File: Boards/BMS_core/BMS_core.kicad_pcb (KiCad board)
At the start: 2 copper layers, 73.7 x 61 mm, 67 parts, among them IC1 ATMEGA16M1, J1 CONN_02X03, J2 B5B-PH-K-S, J3 NanoFit_2, J4 MicroFit_RA_V_2, J5 MM_F_VT_14, K1 G5Q-1A4-DC5-5V, Q1 SSM3K333R, T1 T_LAN_7490100111A, U1 MCP2561-E_SN, U101 TPS561201, U2 SN74LVC1G17, U3 LTC6820HMS, U4 MCP6001, U5 MCP6001, Y1 Crystal_SMD

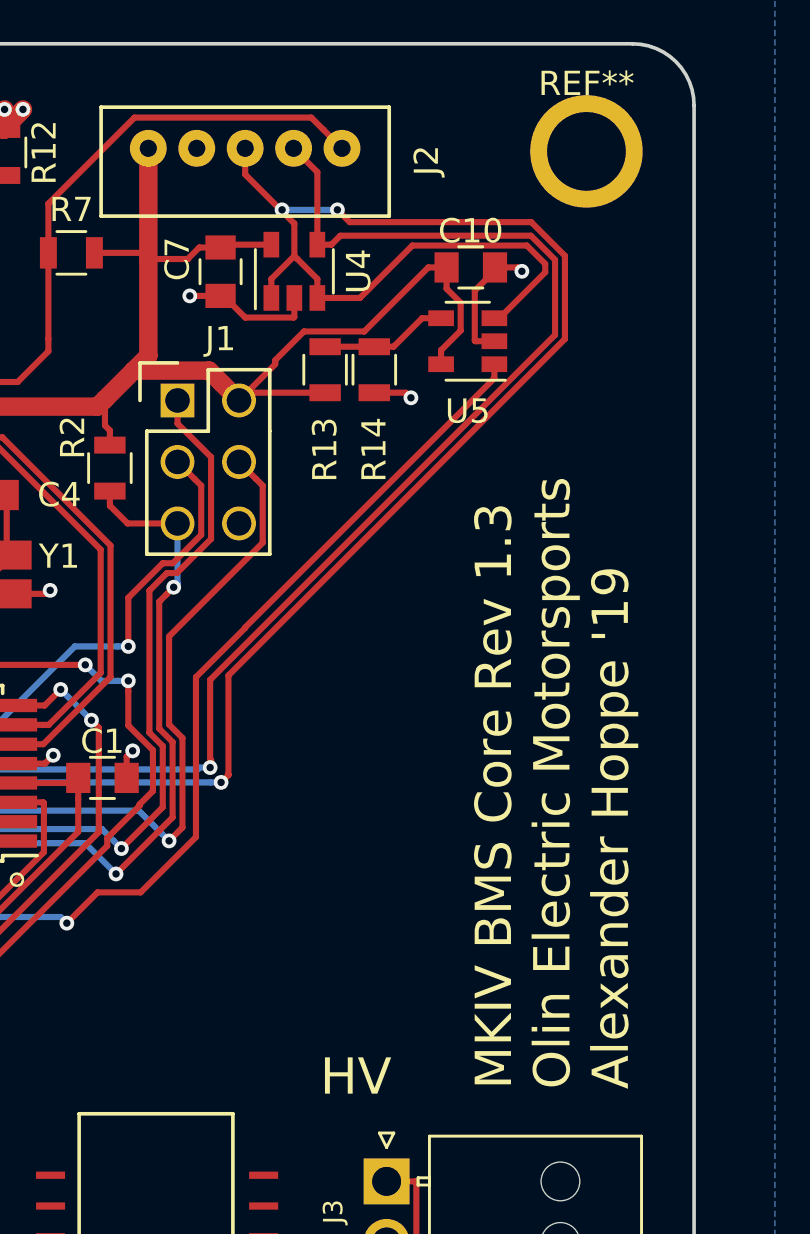
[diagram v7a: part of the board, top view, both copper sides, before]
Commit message: finished layout with new trigger
added components and ran clean DRC
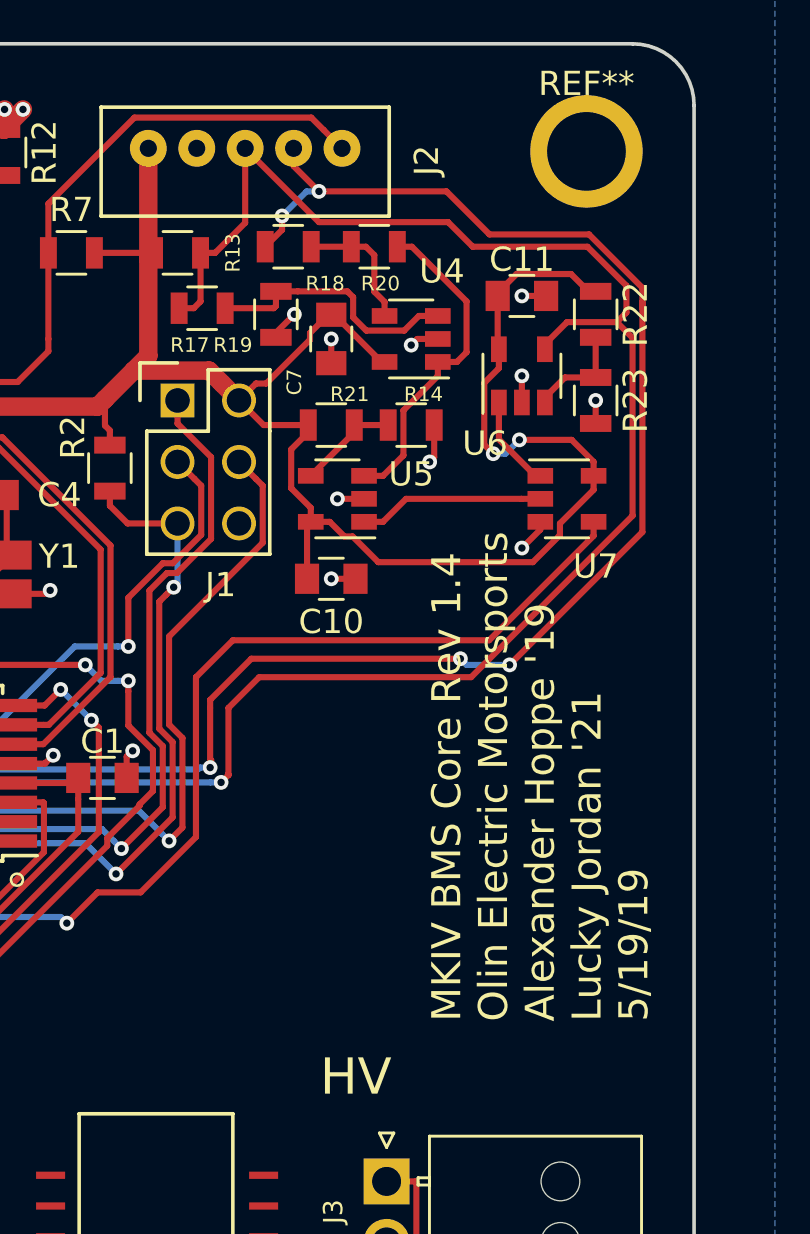
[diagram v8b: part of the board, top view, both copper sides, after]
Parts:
- added C11: C_0.1uF, footprints:C_0805_OEM, F.Cu at (109.7, 58.7)
- added R17: R_10K, footprints:R_0805_OEM, F.Cu at (96.5, 59.2)
- added R18: R_10K, footprints:R_0805_OEM, F.Cu at (100.1, 56.6)
- added R19: R_10K, footprints:R_0805_OEM, F.Cu at (99.6, 59.4)
- added R20: R_10K, footprints:R_0805_OEM, F.Cu at (103.6, 56.6)
- added R21: R_17.8K, footprints:R_0805_OEM, F.Cu at (101.9, 64.0)
- added R22: R_10K, footprints:R_0805_OEM, F.Cu at (112.8, 59.4)
- added R23: R_1K, footprints:R_0805_OEM, F.Cu at (112.8, 63.0)
- added U6: MCP6001, footprints:SOT-23-5_OEM, F.Cu at (109.7, 62.0)
- added U7: SN74LVC1G32, footprints:SOT-23-5_OEM, F.Cu at (111.6, 67.1)
- R13: value R_17.4K_0.1 -> R_10K
- moved C10 14.1 mm to (101.9, 70.4)
- moved U5 8.45 mm to (102.1, 67.1)
- moved R13 7.78 mm to (95.5, 56.9), turned to 180 degrees
- moved U4 5.58 mm to (105.2, 60.5), turned to 180 degrees
- moved C7 5.35 mm to (101.9, 60.5)
- moved R14 2.75 mm to (105.2, 64.0), turned to 0 degrees
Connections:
- R13 pad 1: VCC -> /VOUT
- R13 pad 2: Net-(R13-Pad2) -> VCC
- R14 pad 1: Net-(R13-Pad2) -> Net-(R14-Pad1)
- U4 pad 1: /VOUT -> Net-(R20-Pad2)
- U4 pad 3: /VOUT -> Net-(R17-Pad2)
- U4 pad 4: /VREF -> Net-(R18-Pad2)
- U5 pad 1: /BSPD_CURRENT -> Net-(U5-Pad1)
- U5 pad 3: /VOUT -> Net-(R20-Pad2)
- U5 pad 4: Net-(R13-Pad2) -> Net-(R14-Pad1)
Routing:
- net VCC: track 214.3 -> 240.5 mm, vias 5 -> 7
- net Net-(R20-Pad2): track 0.00 -> 13.7 mm
- net /VREF: track 59.5 -> 72.7 mm, vias 2 -> 6
- net Net-(R17-Pad2): track 0.00 -> 10.8 mm
- net Net-(U5-Pad1): track 0.00 -> 7.68 mm
- net Net-(R18-Pad2): track 0.00 -> 5.44 mm
- net Net-(R13-Pad2): track 5.28 -> 0.00 mm
- net Net-(R22-Pad2): track 0.00 -> 4.30 mm
- net Net-(R14-Pad1): track 0.00 -> 4.24 mm
- net Net-(U6-Pad1): track 0.00 -> 3.86 mm
- net /BSPD_CURRENT: track 78.4 -> 79.8 mm
- net GND: track 69.1 -> 68.3 mm, vias 39 -> 46
- net /VOUT: track 81.4 -> 81.1 mm, vias 4 -> 2
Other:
- board text added: "MKIV BMS Core Rev 1.4 Olin Electric Motorsports Alexander Hoppe '19 Lucky Jordan '21 5/19/19"
- board text removed: "MKIV BMS Core Rev 1.3 Olin Electric Motorsports Alexander Hoppe '19"
